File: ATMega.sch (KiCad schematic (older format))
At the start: 24 parts, among them J5 Conn_02x03_Odd_Even, SW1 SW_Push, U1 ATmega2560-16AU, Y1 16MHz

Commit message: more LEDs
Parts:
- added D5, D6, D7, D8: (no value), LED_SMD:LED_0603_1608Metric, symbol Device:LED_Small
- added R10, R7, R8, R9: 5.6, Resistor_SMD:R_0603_1608Metric, symbol Device:R
- renumbered R7 to R11, R8 to R12, R9 to R13, R10 to R14, R11 to R15
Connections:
- net GND: now also D5.1 (K), D6.1 (K), D7.1 (K), D8.1 (K)
- net at U1.39 (PL4): now also R7.1
- net at U1.40 (PL5): now also R8.1
- net at U1.41 (PL6): now also R9.1
- net at U1.42 (PL7): now also R10.1
- new net: D5.2 (A), R7.2
- new net: D6.2 (A), R8.2
- new net: D7.2 (A), R9.2
- new net: D8.2 (A), R10.2
- no-connect marks 73 -> 69
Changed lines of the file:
@@
 Wire Wire Line
 	2200 2550 2250 2550
-$Comp
-L power:GND #PWR012
-U 1 1 5C284E11
-P 1950 2600
-F 0 "#PWR012" H 1950 2350 50  0001 C CNN
-F 1 "GND" H 1955 2427 50  0000 C CNN
-F 2 "" H 1950 2600 50  0001 C CNN
-F 3 "" H 1950 2600 50  0001 C CNN
-	1    1950 2600
-	1    0    0    -1
-$EndComp
-Wire Wire Line
-	1950 2600 1950 2550
 Wire Wire Line
 	1950 2250 2000 2250
@@
 	1950 2550 1950 2450
 $Comp
-L Device:R R7
+L Device:R R11
 U 1 1 5C28BE77
 P 2550 1100
-F 0 "R7" V 2550 1100 50  0000 C CNN
+F 0 "R11" V 2550 1100 50  0000 C CNN
 F 1 "10k" H 2620 1055 50  0000 L CNN
 F 2 "Resistor_SMD:R_0603_1608Metric" V 2480 1100 50  0001 C CNN
@@
 	4350 4150 4550 4150
 $Comp
-L Device:R R8
+L Device:R R12
 U 1 1 5C325691
 P 4350 3850
-F 0 "R8" V 4350 3850 50  0000 C CNN
+F 0 "R12" V 4350 3850 50  0000 C CNN
 F 1 "10k" H 4420 3805 50  0001 L CNN
 F 2 "Resistor_SMD:R_0603_1608Metric" V 4280 3850 50  0001 C CNN
@@
 $EndComp
 $Comp
-L Device:R R9
+L Device:R R13
 U 1 1 5C325799
 P 4500 3850
-F 0 "R9" V 4500 3850 50  0000 C CNN
+F 0 "R13" V 4500 3850 50  0000 C CNN
 F 1 "10k" H 4570 3805 50  0000 L CNN
 F 2 "Resistor_SMD:R_0603_1608Metric" V 4430 3850 50  0001 C CNN
@@
 3V3IN
 $Comp
-L Device:R_Small R10
+L Device:R_Small R14
 U 1 1 5C32D2D3
 P 4600 5200
-F 0 "R10" V 4600 5200 50  0000 C CNN
+F 0 "R14" V 4600 5200 50  0000 C CNN
 F 1 "10k" H 4659 5155 50  0001 L CNN
 F 2 "Resistor_SMD:R_0603_1608Metric" H 4600 5200 50  0001 C CNN
@@
 $EndComp
 $Comp
-L Device:R_Small R11
+L Device:R_Small R15
 U 1 1 5C32D353
 P 4700 5200
-F 0 "R11" V 4700 5200 50  0000 C CNN
+F 0 "R15" V 4700 5200 50  0000 C CNN
 F 1 "10k" H 4750 5200 50  0000 L CNN
 F 2 "Resistor_SMD:R_0603_1608Metric" H 4700 5200 50  0001 C CNN
@@
 Text HLabel 4700 5000 1    50   Input ~ 0
 3V3IN
-NoConn ~ 2650 2650
-NoConn ~ 2650 2750
-NoConn ~ 2650 2850
-NoConn ~ 2650 2950
 NoConn ~ 2650 3150
 NoConn ~ 2650 3250
@@
 	1    0    0    -1
 $EndComp
+$Comp
+L Device:R R7
+U 1 1 5CAADA8E
+P 2400 2650
+F 0 "R7" V 2400 2650 50  0000 C CNN
+F 1 "5.6" V 2450 2850 50  0000 C CNN
+F 2 "Resistor_SMD:R_0603_1608Metric" V 2330 2650 50  0001 C CNN
+F 3 "~" H 2400 2650 50  0001 C CNN
+	1    2400 2650
+	0    1    1    0
+$EndComp
+$Comp
+L Device:R R8
+U 1 1 5CAADA94
+P 2400 2750
+F 0 "R8" V 2400 2750 50  0000 C CNN
+F 1 "5.6" V 2450 2950 50  0000 C CNN
+F 2 "Resistor_SMD:R_0603_1608Metric" V 2330 2750 50  0001 C CNN
+F 3 "~" H 2400 2750 50  0001 C CNN
+	1    2400 2750
+	0    1    1    0
+$EndComp
+$Comp
+L Device:R R9
+U 1 1 5CAADA9A
+P 2400 2850
+F 0 "R9" V 2400 2850 50  0000 C CNN
+F 1 "5.6" V 2450 3050 50  0000 C CNN
+F 2 "Resistor_SMD:R_0603_1608Metric" V 2330 2850 50  0001 C CNN
+F 3 "~" H 2400 2850 50  0001 C CNN
+	1    2400 2850
+	0    1    1    0
+$EndComp
+$Comp
+L Device:R R10
+U 1 1 5CAADAA0
+P 2400 2950
+F 0 "R10" V 2400 2950 50  0000 C CNN
+F 1 "5.6" V 2450 3150 50  0000 C CNN
+F 2 "Resistor_SMD:R_0603_1608Metric" V 2330 2950 50  0001 C CNN
+F 3 "~" H 2400 2950 50  0001 C CNN
+	1    2400 2950
+	0    1    1    0
+$EndComp
+Wire Wire Line
+	2650 2650 2550 2650
+Wire Wire Line
+	2550 2750 2650 2750
+Wire Wire Line
+	2550 2850 2650 2850
+Wire Wire Line
+	2550 2950 2650 2950
+$Comp
+L Device:LED_Small D5
+U 1 1 5CAADAAA
+P 2100 2650
+F 0 "D5" H 2200 2600 50  0000 C CNN
+F 1 " " H 1750 2750 50  0000 C CNN
+F 2 "LED_SMD:LED_0603_1608Metric" V 2100 2650 50  0001 C CNN
+F 3 "~" V 2100 2650 50  0001 C CNN
+	1    2100 2650
+	1    0    0    -1
+$EndComp
+$Comp
+L Device:LED_Small D6
+U 1 1 5CAADAB0
+P 2100 2750
+F 0 "D6" H 2200 2700 50  0000 C CNN
+F 1 " " H 2100 2894 50  0000 C CNN
+F 2 "LED_SMD:LED_0603_1608Metric" V 2100 2750 50  0001 C CNN
+F 3 "~" V 2100 2750 50  0001 C CNN
+	1    2100 2750
+	1    0    0    -1
+$EndComp
+$Comp
+L Device:LED_Small D7
+U 1 1 5CAADAB6
+P 2100 2850
+F 0 "D7" H 2200 2800 50  0000 C CNN
+F 1 " " H 2100 2994 50  0000 C CNN
+F 2 "LED_SMD:LED_0603_1608Metric" V 2100 2850 50  0001 C CNN
+F 3 "~" V 2100 2850 50  0001 C CNN
+	1    2100 2850
+	1    0    0    -1
+$EndComp
+$Comp
+L Device:LED_Small D8
+U 1 1 5CAADABC
+P 2100 2950
+F 0 "D8" H 2200 2900 50  0000 C CNN
+F 1 " " H 2100 3094 50  0000 C CNN
+F 2 "LED_SMD:LED_0603_1608Metric" V 2100 2950 50  0001 C CNN
+F 3 "~" V 2100 2950 50  0001 C CNN
+	1    2100 2950
+	1    0    0    -1
+$EndComp
+Wire Wire Line
+	2200 2650 2250 2650
+Wire Wire Line
+	2250 2750 2200 2750
+Wire Wire Line
+	2200 2850 2250 2850
+Wire Wire Line
+	2200 2950 2250 2950
+$Comp
+L power:GND #PWR012
+U 1 1 5CAADAC6
+P 1950 3000
+F 0 "#PWR012" H 1950 2750 50  0001 C CNN
+F 1 "GND" H 1955 2827 50  0000 C CNN
+F 2 "" H 1950 3000 50  0001 C CNN
+F 3 "" H 1950 3000 50  0001 C CNN
+	1    1950 3000
+	1    0    0    -1
+$EndComp
+Wire Wire Line
+	1950 3000 1950 2950
+Wire Wire Line
+	1950 2650 2000 2650
+Wire Wire Line
+	2000 2750 1950 2750
+Connection ~ 1950 2750
+Wire Wire Line
+	1950 2750 1950 2650
+Wire Wire Line
+	2000 2850 1950 2850
+Connection ~ 1950 2850
+Wire Wire Line
+	1950 2850 1950 2750
+Wire Wire Line
+	2000 2950 1950 2950
+Connection ~ 1950 2950
+Wire Wire Line
+	1950 2950 1950 2850
+Wire Wire Line
+	1950 2550 1950 2650
+Connection ~ 1950 2650
 $EndSCHEMATC

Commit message: layout
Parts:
- renumbered J5 to J9
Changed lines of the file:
@@
 	3450 1000 3450 950
 $Comp
-L power:GND #PWR014
+L power:GND #PWR023
 U 1 1 5C280F6E
 P 3450 6950
-F 0 "#PWR014" H 3450 6700 50  0001 C CNN
+F 0 "#PWR023" H 3450 6700 50  0001 C CNN
 F 1 "GND" H 3455 6777 50  0000 C CNN
 F 2 "" H 3450 6950 50  0001 C CNN
@@
 	2100 1750 2150 1750
 $Comp
-L power:GND #PWR013
+L power:GND #PWR022
 U 1 1 5C28167C
 P 2100 1850
-F 0 "#PWR013" H 2100 1600 50  0001 C CNN
+F 0 "#PWR022" H 2100 1600 50  0001 C CNN
 F 1 "GND" H 2105 1677 50  0000 C CNN
 F 2 "" H 2100 1850 50  0001 C CNN
@@
 	5750 1250 6150 1250
 $Comp
-L power:GND #PWR015
+L power:GND #PWR024
 U 1 1 5C29743D
 P 6150 1600
-F 0 "#PWR015" H 6150 1350 50  0001 C CNN
+F 0 "#PWR024" H 6150 1350 50  0001 C CNN
 F 1 "GND" H 6155 1427 50  0000 C CNN
 F 2 "" H 6150 1600 50  0001 C CNN
@@
 	6150 1250 6150 1200
 $Comp
-L Connector_Generic:Conn_02x03_Odd_Even J5
+L Connector_Generic:Conn_02x03_Odd_Even J9
 U 1 1 5C29DEFC
 P 8450 2450
-F 0 "J5" H 8500 2767 50  0000 C CNN
+F 0 "J9" H 8500 2767 50  0000 C CNN
 F 1 "Conn_02x03_Odd_Even" H 8500 2676 50  0000 C CNN
 F 2 "Connector_PinHeader_2.54mm:PinHeader_2x03_P2.54mm_Vertical" H 8450 2450 50  0001 C CNN
@@
 MOSI
 $Comp
-L power:GND #PWR016
+L power:GND #PWR025
 U 1 1 5C2A1657
 P 8800 2650
-F 0 "#PWR016" H 8800 2400 50  0001 C CNN
+F 0 "#PWR025" H 8800 2400 50  0001 C CNN
 F 1 "GND" H 8805 2477 50  0000 C CNN
 F 2 "" H 8800 2650 50  0001 C CNN
@@
 	1650 1300 1650 1350
 $Comp
-L power:GND #PWR011
+L power:GND #PWR020
 U 1 1 5CA944A5
 P 1650 1350
-F 0 "#PWR011" H 1650 1100 50  0001 C CNN
+F 0 "#PWR020" H 1650 1100 50  0001 C CNN
 F 1 "GND" H 1655 1177 50  0000 C CNN
 F 2 "" H 1650 1350 50  0001 C CNN
@@
 	2200 2950 2250 2950
 $Comp
-L power:GND #PWR012
+L power:GND #PWR021
 U 1 1 5CAADAC6
 P 1950 3000
-F 0 "#PWR012" H 1950 2750 50  0001 C CNN
+F 0 "#PWR021" H 1950 2750 50  0001 C CNN
 F 1 "GND" H 1955 2827 50  0000 C CNN
 F 2 "" H 1950 3000 50  0001 C CNN

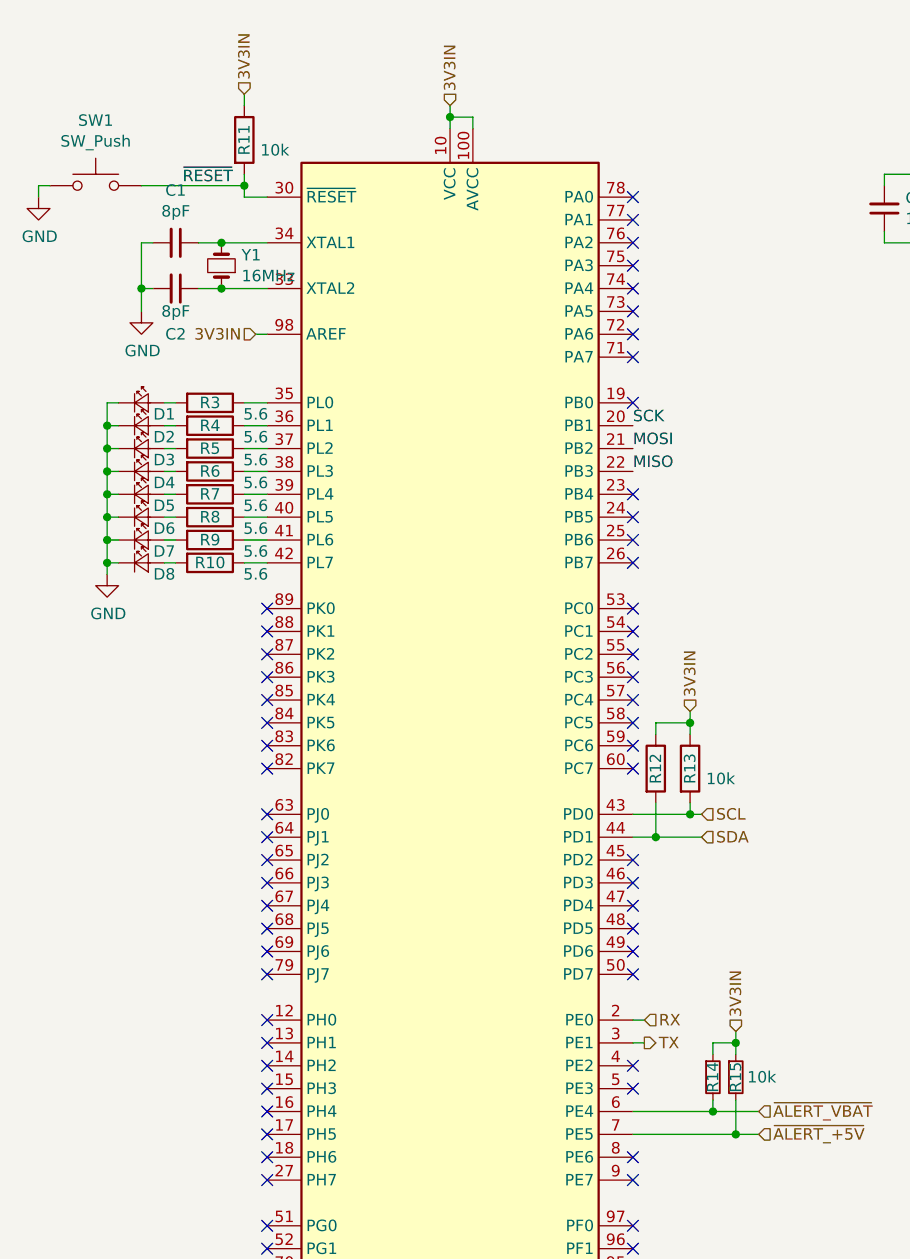
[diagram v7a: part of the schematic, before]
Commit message: layout fixes, reannotate
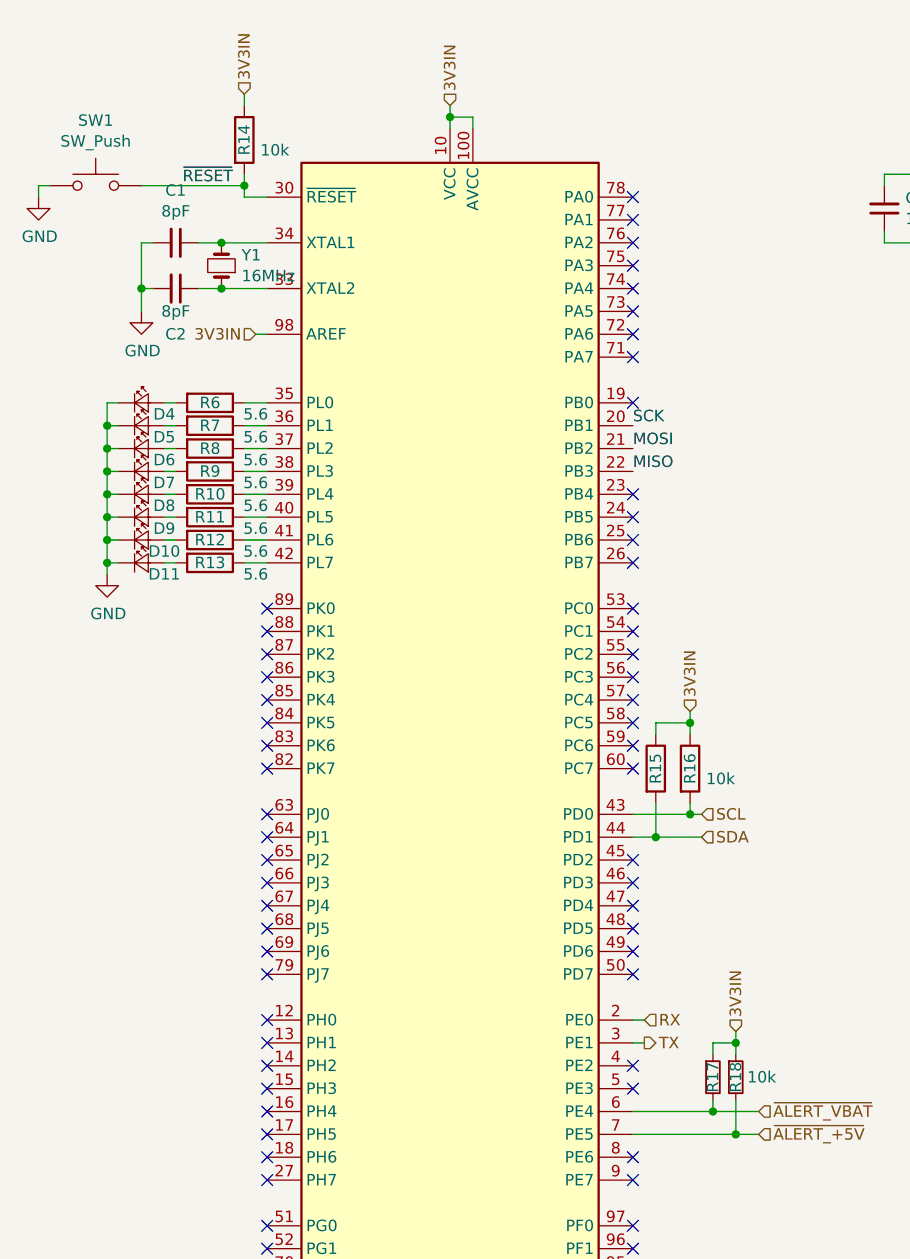
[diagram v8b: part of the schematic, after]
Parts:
- renumbered D7 to D10, D8 to D11, D1 to D4, D2 to D5, D3 to D6, D4 to D7, D5 to D8, D6 to D9, R7 to R10, R8 to R11, R9 to R12, R10 to R13, R11 to R14, R12 to R15, R13 to R16, R14 to R17, R15 to R18, R3 to R6, R4 to R7, R5 to R8, R6 to R9
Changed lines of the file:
@@
 	3450 1000 3450 950
 $Comp
-L power:GND #PWR023
+L power:GND #PWR032
 U 1 1 5C280F6E
 P 3450 6950
-F 0 "#PWR023" H 3450 6700 50  0001 C CNN
+F 0 "#PWR032" H 3450 6700 50  0001 C CNN
 F 1 "GND" H 3455 6777 50  0000 C CNN
 F 2 "" H 3450 6950 50  0001 C CNN
@@
 	2100 1750 2150 1750
 $Comp
-L power:GND #PWR022
+L power:GND #PWR031
 U 1 1 5C28167C
 P 2100 1850
-F 0 "#PWR022" H 2100 1600 50  0001 C CNN
+F 0 "#PWR031" H 2100 1600 50  0001 C CNN
 F 1 "GND" H 2105 1677 50  0000 C CNN
 F 2 "" H 2100 1850 50  0001 C CNN
@@
 Connection ~ 2100 1750
 $Comp
-L Device:R R3
+L Device:R R6
 U 1 1 5C281CF1
 P 2400 2250
-F 0 "R3" V 2400 2250 50  0000 C CNN
+F 0 "R6" V 2400 2250 50  0000 C CNN
 F 1 "5.6" V 2450 2450 50  0000 C CNN
 F 2 "Resistor_SMD:R_0603_1608Metric" V 2330 2250 50  0001 C CNN
@@
 $EndComp
 $Comp
-L Device:R R4
+L Device:R R7
 U 1 1 5C281E2C
 P 2400 2350
-F 0 "R4" V 2400 2350 50  0000 C CNN
+F 0 "R7" V 2400 2350 50  0000 C CNN
 F 1 "5.6" V 2450 2550 50  0000 C CNN
 F 2 "Resistor_SMD:R_0603_1608Metric" V 2330 2350 50  0001 C CNN
@@
 $EndComp
 $Comp
-L Device:R R5
+L Device:R R8
 U 1 1 5C281E58
 P 2400 2450
-F 0 "R5" V 2400 2450 50  0000 C CNN
+F 0 "R8" V 2400 2450 50  0000 C CNN
 F 1 "5.6" V 2450 2650 50  0000 C CNN
 F 2 "Resistor_SMD:R_0603_1608Metric" V 2330 2450 50  0001 C CNN
@@
 $EndComp
 $Comp
-L Device:R R6
+L Device:R R9
 U 1 1 5C281E76
 P 2400 2550
-F 0 "R6" V 2400 2550 50  0000 C CNN
+F 0 "R9" V 2400 2550 50  0000 C CNN
 F 1 "5.6" V 2450 2750 50  0000 C CNN
 F 2 "Resistor_SMD:R_0603_1608Metric" V 2330 2550 50  0001 C CNN
@@
 	2550 2550 2650 2550
 $Comp
-L Device:LED_Small D1
+L Device:LED_Small D4
 U 1 1 5C2825A8
 P 2100 2250
-F 0 "D1" H 2200 2200 50  0000 C CNN
+F 0 "D4" H 2200 2200 50  0000 C CNN
 F 1 " " H 1750 2350 50  0000 C CNN
 F 2 "LED_SMD:LED_0603_1608Metric" V 2100 2250 50  0001 C CNN
@@
 $EndComp
 $Comp
-L Device:LED_Small D2
+L Device:LED_Small D5
 U 1 1 5C2825D4
 P 2100 2350
-F 0 "D2" H 2200 2300 50  0000 C CNN
+F 0 "D5" H 2200 2300 50  0000 C CNN
 F 1 " " H 2100 2494 50  0000 C CNN
 F 2 "LED_SMD:LED_0603_1608Metric" V 2100 2350 50  0001 C CNN
@@
 $EndComp
 $Comp
-L Device:LED_Small D3
+L Device:LED_Small D6
 U 1 1 5C2825F8
 P 2100 2450
-F 0 "D3" H 2200 2400 50  0000 C CNN
+F 0 "D6" H 2200 2400 50  0000 C CNN
 F 1 " " H 2100 2594 50  0000 C CNN
 F 2 "LED_SMD:LED_0603_1608Metric" V 2100 2450 50  0001 C CNN
@@
 $EndComp
 $Comp
-L Device:LED_Small D4
+L Device:LED_Small D7
 U 1 1 5C282622
 P 2100 2550
-F 0 "D4" H 2200 2500 50  0000 C CNN
+F 0 "D7" H 2200 2500 50  0000 C CNN
 F 1 " " H 2100 2694 50  0000 C CNN
 F 2 "LED_SMD:LED_0603_1608Metric" V 2100 2550 50  0001 C CNN
@@
 	1950 2550 1950 2450
 $Comp
-L Device:R R11
+L Device:R R14
 U 1 1 5C28BE77
 P 2550 1100
-F 0 "R11" V 2550 1100 50  0000 C CNN
+F 0 "R14" V 2550 1100 50  0000 C CNN
 F 1 "10k" H 2620 1055 50  0000 L CNN
 F 2 "Resistor_SMD:R_0603_1608Metric" V 2480 1100 50  0001 C CNN
@@
 	5750 1250 6150 1250
 $Comp
-L power:GND #PWR024
+L power:GND #PWR033
 U 1 1 5C29743D
 P 6150 1600
-F 0 "#PWR024" H 6150 1350 50  0001 C CNN
+F 0 "#PWR033" H 6150 1350 50  0001 C CNN
 F 1 "GND" H 6155 1427 50  0000 C CNN
 F 2 "" H 6150 1600 50  0001 C CNN
@@
 MOSI
 $Comp
-L power:GND #PWR025
+L power:GND #PWR034
 U 1 1 5C2A1657
 P 8800 2650
-F 0 "#PWR025" H 8800 2400 50  0001 C CNN
+F 0 "#PWR034" H 8800 2400 50  0001 C CNN
 F 1 "GND" H 8805 2477 50  0000 C CNN
 F 2 "" H 8800 2650 50  0001 C CNN
@@
 	4350 4150 4550 4150
 $Comp
-L Device:R R12
+L Device:R R15
 U 1 1 5C325691
 P 4350 3850
-F 0 "R12" V 4350 3850 50  0000 C CNN
+F 0 "R15" V 4350 3850 50  0000 C CNN
 F 1 "10k" H 4420 3805 50  0001 L CNN
 F 2 "Resistor_SMD:R_0603_1608Metric" V 4280 3850 50  0001 C CNN
@@
 $EndComp
 $Comp
-L Device:R R13
+L Device:R R16
 U 1 1 5C325799
 P 4500 3850
-F 0 "R13" V 4500 3850 50  0000 C CNN
+F 0 "R16" V 4500 3850 50  0000 C CNN
 F 1 "10k" H 4570 3805 50  0000 L CNN
 F 2 "Resistor_SMD:R_0603_1608Metric" V 4430 3850 50  0001 C CNN
@@
 3V3IN
 $Comp
-L Device:R_Small R14
+L Device:R_Small R17
 U 1 1 5C32D2D3
 P 4600 5200
-F 0 "R14" V 4600 5200 50  0000 C CNN
+F 0 "R17" V 4600 5200 50  0000 C CNN
 F 1 "10k" H 4659 5155 50  0001 L CNN
 F 2 "Resistor_SMD:R_0603_1608Metric" H 4600 5200 50  0001 C CNN
@@
 $EndComp
 $Comp
-L Device:R_Small R15
+L Device:R_Small R18
 U 1 1 5C32D353
 P 4700 5200
-F 0 "R15" V 4700 5200 50  0000 C CNN
+F 0 "R18" V 4700 5200 50  0000 C CNN
 F 1 "10k" H 4750 5200 50  0000 L CNN
 F 2 "Resistor_SMD:R_0603_1608Metric" H 4700 5200 50  0001 C CNN
@@
 	1650 1300 1650 1350
 $Comp
-L power:GND #PWR020
+L power:GND #PWR029
 U 1 1 5CA944A5
 P 1650 1350
-F 0 "#PWR020" H 1650 1100 50  0001 C CNN
+F 0 "#PWR029" H 1650 1100 50  0001 C CNN
 F 1 "GND" H 1655 1177 50  0000 C CNN
 F 2 "" H 1650 1350 50  0001 C CNN
@@
 $EndComp
 $Comp
-L Device:R R7
+L Device:R R10
 U 1 1 5CAADA8E
 P 2400 2650
-F 0 "R7" V 2400 2650 50  0000 C CNN
+F 0 "R10" V 2400 2650 50  0000 C CNN
 F 1 "5.6" V 2450 2850 50  0000 C CNN
 F 2 "Resistor_SMD:R_0603_1608Metric" V 2330 2650 50  0001 C CNN
@@
 $EndComp
 $Comp
-L Device:R R8
+L Device:R R11
 U 1 1 5CAADA94
 P 2400 2750
-F 0 "R8" V 2400 2750 50  0000 C CNN
+F 0 "R11" V 2400 2750 50  0000 C CNN
 F 1 "5.6" V 2450 2950 50  0000 C CNN
 F 2 "Resistor_SMD:R_0603_1608Metric" V 2330 2750 50  0001 C CNN
@@
 $EndComp
 $Comp
-L Device:R R9
+L Device:R R12
 U 1 1 5CAADA9A
 P 2400 2850
-F 0 "R9" V 2400 2850 50  0000 C CNN
+F 0 "R12" V 2400 2850 50  0000 C CNN
 F 1 "5.6" V 2450 3050 50  0000 C CNN
 F 2 "Resistor_SMD:R_0603_1608Metric" V 2330 2850 50  0001 C CNN
@@
 $EndComp
 $Comp
-L Device:R R10
+L Device:R R13
 U 1 1 5CAADAA0
 P 2400 2950
-F 0 "R10" V 2400 2950 50  0000 C CNN
+F 0 "R13" V 2400 2950 50  0000 C CNN
 F 1 "5.6" V 2450 3150 50  0000 C CNN
 F 2 "Resistor_SMD:R_0603_1608Metric" V 2330 2950 50  0001 C CNN
@@
 	2550 2950 2650 2950
 $Comp
-L Device:LED_Small D5
+L Device:LED_Small D8
 U 1 1 5CAADAAA
 P 2100 2650
-F 0 "D5" H 2200 2600 50  0000 C CNN
+F 0 "D8" H 2200 2600 50  0000 C CNN
 F 1 " " H 1750 2750 50  0000 C CNN
 F 2 "LED_SMD:LED_0603_1608Metric" V 2100 2650 50  0001 C CNN
@@
 $EndComp
 $Comp
-L Device:LED_Small D6
+L Device:LED_Small D9
 U 1 1 5CAADAB0
 P 2100 2750
-F 0 "D6" H 2200 2700 50  0000 C CNN
+F 0 "D9" H 2200 2700 50  0000 C CNN
 F 1 " " H 2100 2894 50  0000 C CNN
 F 2 "LED_SMD:LED_0603_1608Metric" V 2100 2750 50  0001 C CNN
@@
 $EndComp
 $Comp
-L Device:LED_Small D7
+L Device:LED_Small D10
 U 1 1 5CAADAB6
 P 2100 2850
-F 0 "D7" H 2200 2800 50  0000 C CNN
+F 0 "D10" H 2200 2800 50  0000 C CNN
 F 1 " " H 2100 2994 50  0000 C CNN
 F 2 "LED_SMD:LED_0603_1608Metric" V 2100 2850 50  0001 C CNN
@@
 $EndComp
 $Comp
-L Device:LED_Small D8
+L Device:LED_Small D11
 U 1 1 5CAADABC
 P 2100 2950
-F 0 "D8" H 2200 2900 50  0000 C CNN
+F 0 "D11" H 2200 2900 50  0000 C CNN
 F 1 " " H 2100 3094 50  0000 C CNN
 F 2 "LED_SMD:LED_0603_1608Metric" V 2100 2950 50  0001 C CNN
@@
 	2200 2950 2250 2950
 $Comp
-L power:GND #PWR021
+L power:GND #PWR030
 U 1 1 5CAADAC6
 P 1950 3000
-F 0 "#PWR021" H 1950 2750 50  0001 C CNN
+F 0 "#PWR030" H 1950 2750 50  0001 C CNN
 F 1 "GND" H 1955 2827 50  0000 C CNN
 F 2 "" H 1950 3000 50  0001 C CNN
